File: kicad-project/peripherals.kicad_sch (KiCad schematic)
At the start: 26 parts, among them J15 Conn_01x04, J16 Conn_01x02_Female, J17 Conn_01x02_Female, J18 Conn_02x04_Odd_Even, J19 Conn_01x02_Female, J20 Conn_01x02_Female, Q1 S8050, Q2 S8050, Q3 S8050, Q4 S8050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

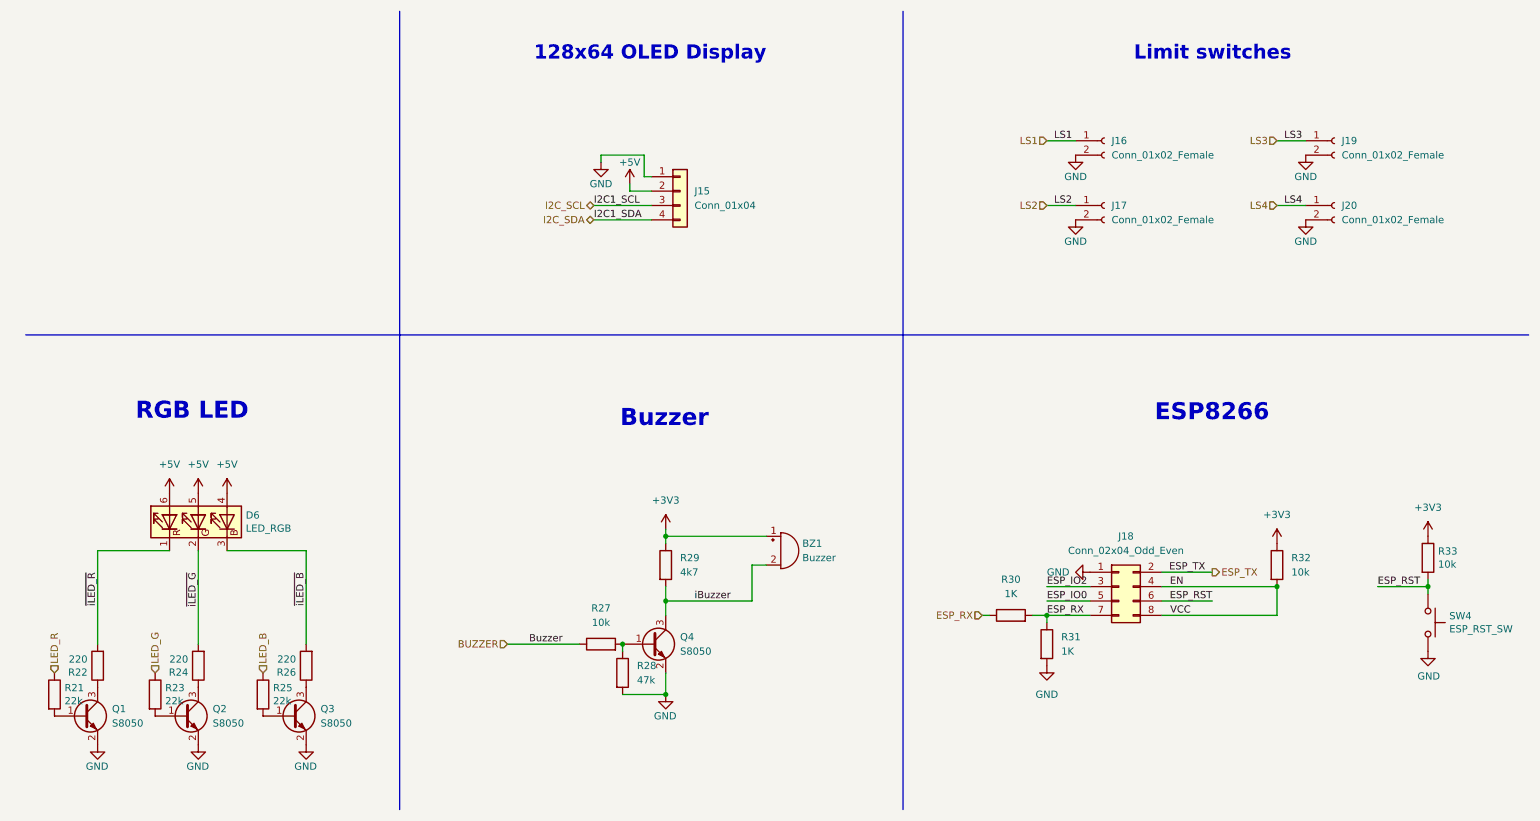
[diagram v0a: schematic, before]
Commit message: hw: finish schematic, PS i2c R_pull-up wrong
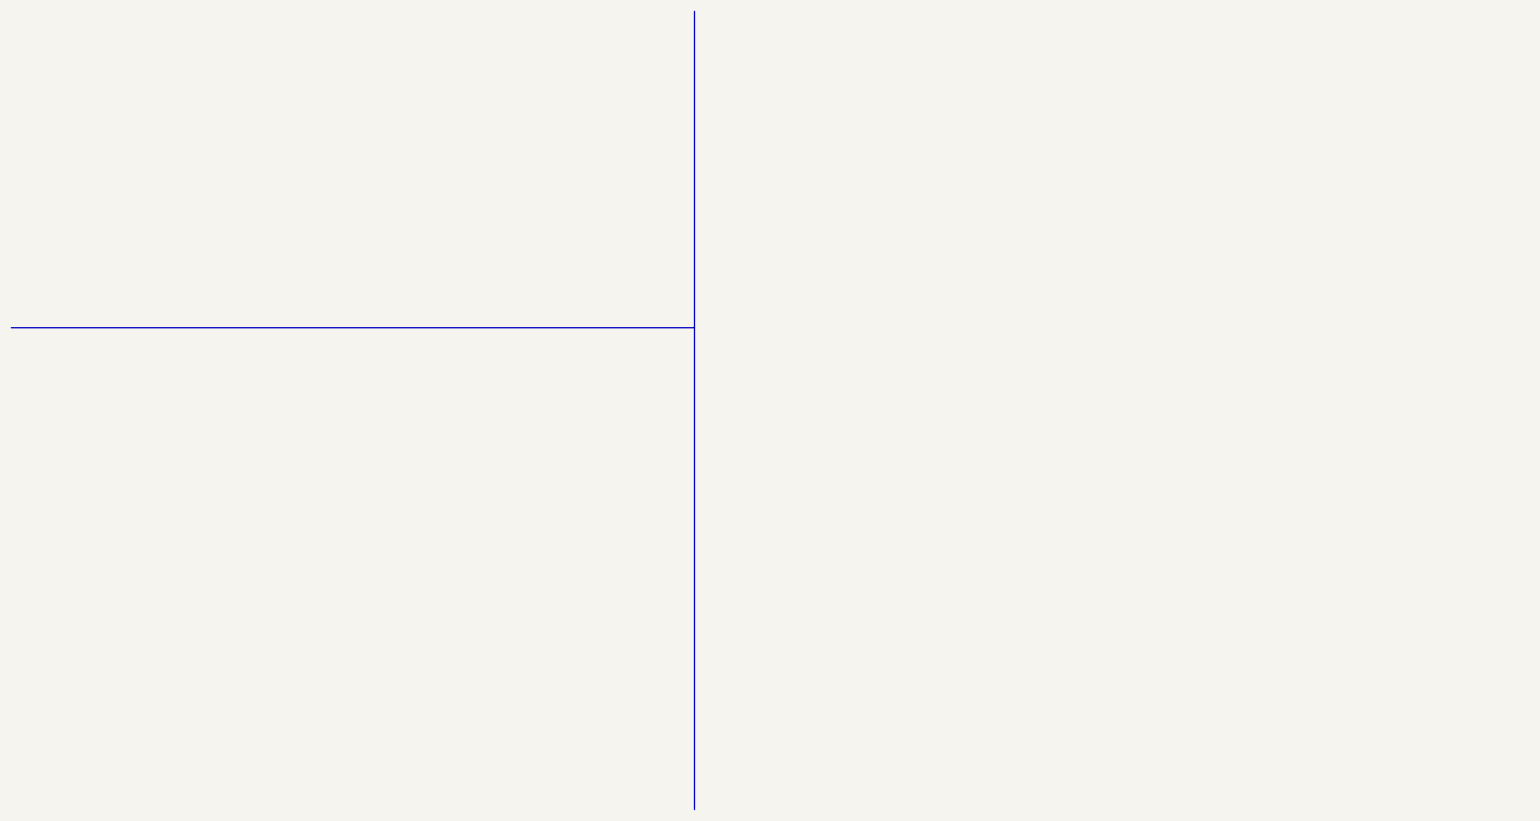
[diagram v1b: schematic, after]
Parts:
- removed BZ1: Buzzer, Buzzer_Beeper:Buzzer_12x9.5RM7.6, symbol Device:Buzzer
- removed D6: LED_RGB, LED_SMD:LED_RGB_1210, symbol Device:LED_RGB
- removed J15: Conn_01x04, Connector_PinHeader_2.54mm:PinHeader_1x04_P2.54mm_Vertical_SMD_Pin1Left, symbol Connector_Generic:Conn_01x04
- removed J16, J17, J19, J20: Conn_01x02_Female, symbol Connector:Conn_01x02_Female
- removed J18: Conn_02x04_Odd_Even, symbol Connector_Generic:Conn_02x04_Odd_Even
- removed Q1, Q2, Q3, Q4: S8050, Package_TO_SOT_SMD:SOT-23, symbol Device:Q_NPN_BEC
- removed R21, R23, R25: 22k, Resistor_SMD:R_0603_1608Metric, symbol Device:R
- removed R22, R24, R26: 220, Resistor_SMD:R_0603_1608Metric, symbol Device:R
- removed R27, R32: 10k, symbol Device:R
- removed R28: 47k, symbol Device:R
- removed R29: 4k7, Resistor_SMD:R_0603_1608Metric, symbol Device:R
- removed R30, R31: 1K, symbol Device:R
- removed R33: 10k, Resistor_SMD:R_0603_1608Metric, symbol Device:R
- removed SW4: ESP_RST_SW, Button_Switch_THT:SW_PUSH_6mm_H4.3mm, symbol Switch:SW_Push
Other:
- note removed: "128x64 OLED Display"
- note removed: "Buzzer"
- note removed: "ESP8266"
- note removed: "Limit switches"
- note removed: "RGB LED"
